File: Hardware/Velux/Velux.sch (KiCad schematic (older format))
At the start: 24 parts, among them J1 5VIN, J2 Conn_01x02_Female, J3 Velux_OUT, J4 24V_IN, J5 FLASH, K1 UMS05-1A80-75L, K2 SANYOU_SRD_Form_C, K3 SANYOU_SRD_Form_C, SW1 RESET, SW2 FLASH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

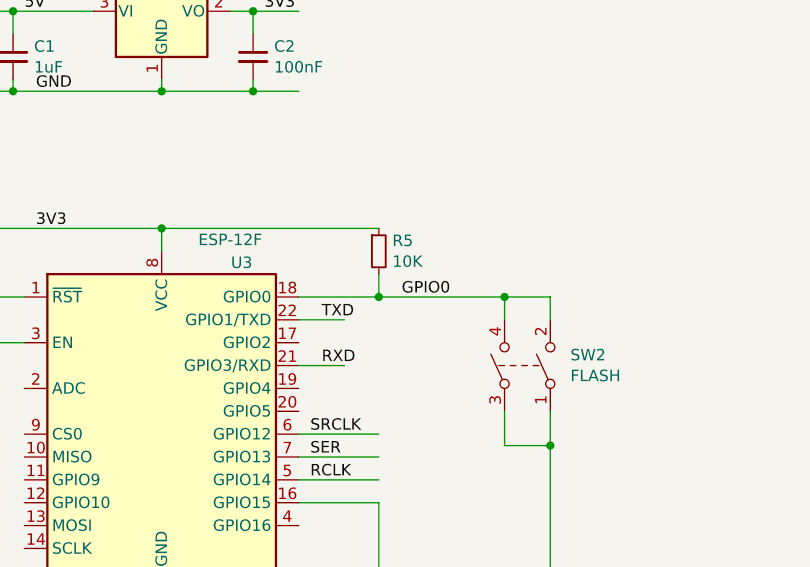
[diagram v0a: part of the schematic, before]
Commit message: - Modified almost all hardware boards : They were missing a pull-up resistor on GPIO2, which made impossible to flash. - Updated baseBoard.* files
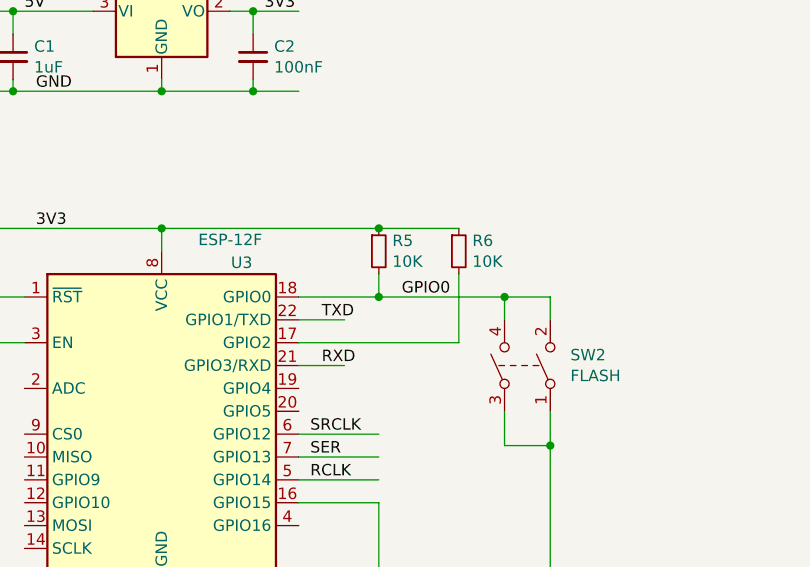
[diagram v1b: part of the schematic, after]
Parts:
- added R6: 10K, Resistor_SMD:R_0805_2012Metric_Pad1.15x1.40mm_HandSolder, symbol Device:R_Small
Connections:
- wire segments 117 -> 120
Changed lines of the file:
@@
 Wire Wire Line
 	3550 2000 3750 2000
+$Comp
+L Device:R_Small R6
+U 1 1 5C84F39A
+P 3350 1800
+F 0 "R6" H 3409 1846 50  0000 L CNN
+F 1 "10K" H 3409 1755 50  0000 L CNN
+F 2 "Resistor_SMD:R_0805_2012Metric_Pad1.15x1.40mm_HandSolder" H 3350 1800 50  0001 C CNN
+F 3 "~" H 3350 1800 50  0001 C CNN
+	1    3350 1800
+	1    0    0    -1
+$EndComp
+Wire Wire Line
+	3000 1700 3350 1700
+Connection ~ 3000 1700
+Wire Wire Line
+	3350 1900 3350 2200
+Wire Wire Line
+	3350 2200 2650 2200
 $EndSCHEMATC
